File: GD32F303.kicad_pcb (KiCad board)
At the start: 4 copper layers, 127 parts, among them CN1 KF128L-5.08-2P, CN2 WJ15EDGRC-3.81-2P, CN4 WJ15EDGRC-3.81-2P, J1 TYPE-C-31-M-31, J2 TYPE-C 16PIN 2MD(073), Q1 CJ3134K KF, Q2 CJ3134K KF, SW1 SKRPACE010, U1 XL1509-5.0, U10 SIT3485ESA, U11 TXS0104EPWR, U12 TXS0104EPWR, U13 CH340E, U14 TPD4S012DRYR, U2 B0503S-2WR3L, U3 SY8089A1AAC, U4 CH213K, U5 SY8089AAC, U6 GD32F303VCT6, U7 ISO1050DWR, U9 π131U30, Y1 TAXM8M4RDBCCT2T, Y2 XKXGI-SUA-32.768K

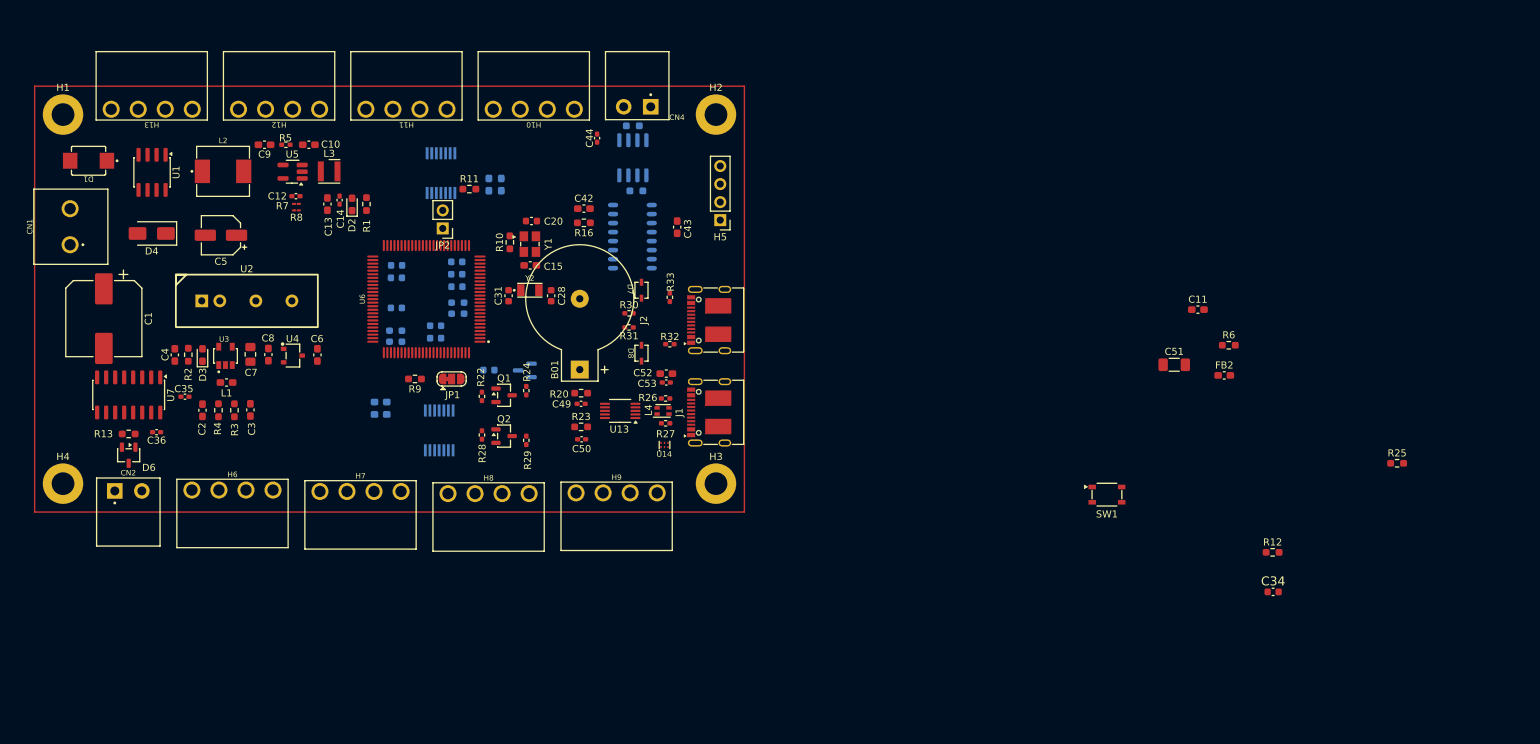
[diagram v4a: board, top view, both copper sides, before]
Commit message: 保存最新器件布局调整
- 归位按键及MCU周边阻容器件
- 调整局部器件方向与丝印位置
- 集中GND与CHASSIS跨接器件等待后续优化
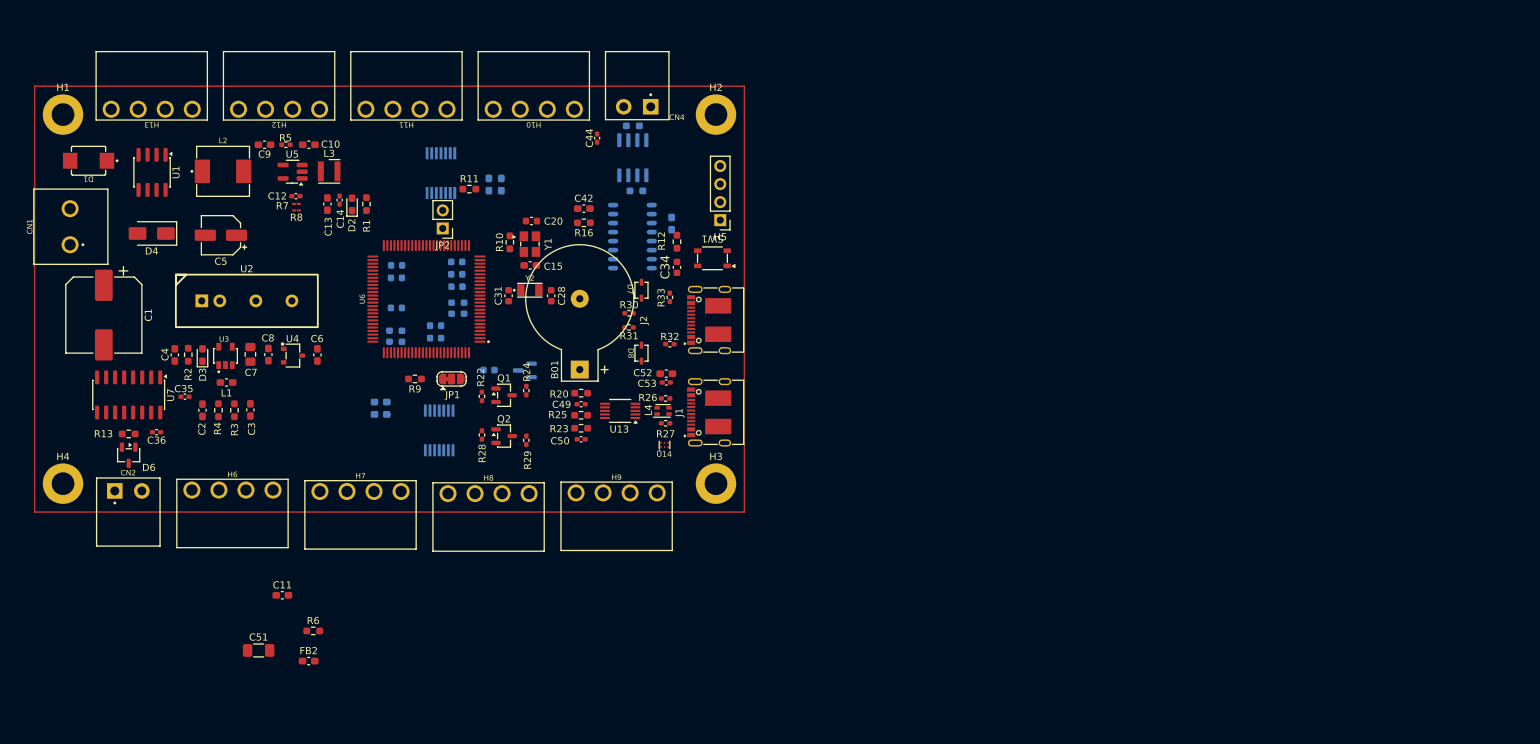
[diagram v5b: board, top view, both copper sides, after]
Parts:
- C43: moved to B.Cu
- moved C51 135.1 mm to (117.1, 138.5)
- moved FB2 135.1 mm to (124.1, 140.0)
- moved R6 135.1 mm to (124.8, 135.8)
- moved C11 135.1 mm to (120.4, 130.7)
- moved R25 115.2 mm to (162.5, 105.4)
- moved C34 95.6 mm to (176.0, 84.5), turned to -90 degrees
- moved R12 94.7 mm to (176.0, 80.9), turned to 90 degrees
- moved SW1 64.8 mm to (181.0, 83.2), turned to 180 degrees
- moved C43 0.93 mm to (175.2, 78.4)
- moved C1 0.50 mm to (95.2, 91.2)
- moved R23 0.19 mm to (162.5, 107.2)
- moved C50 0.07 mm to (162.5, 108.8)
- moved C49 0.06 mm to (162.5, 103.8)

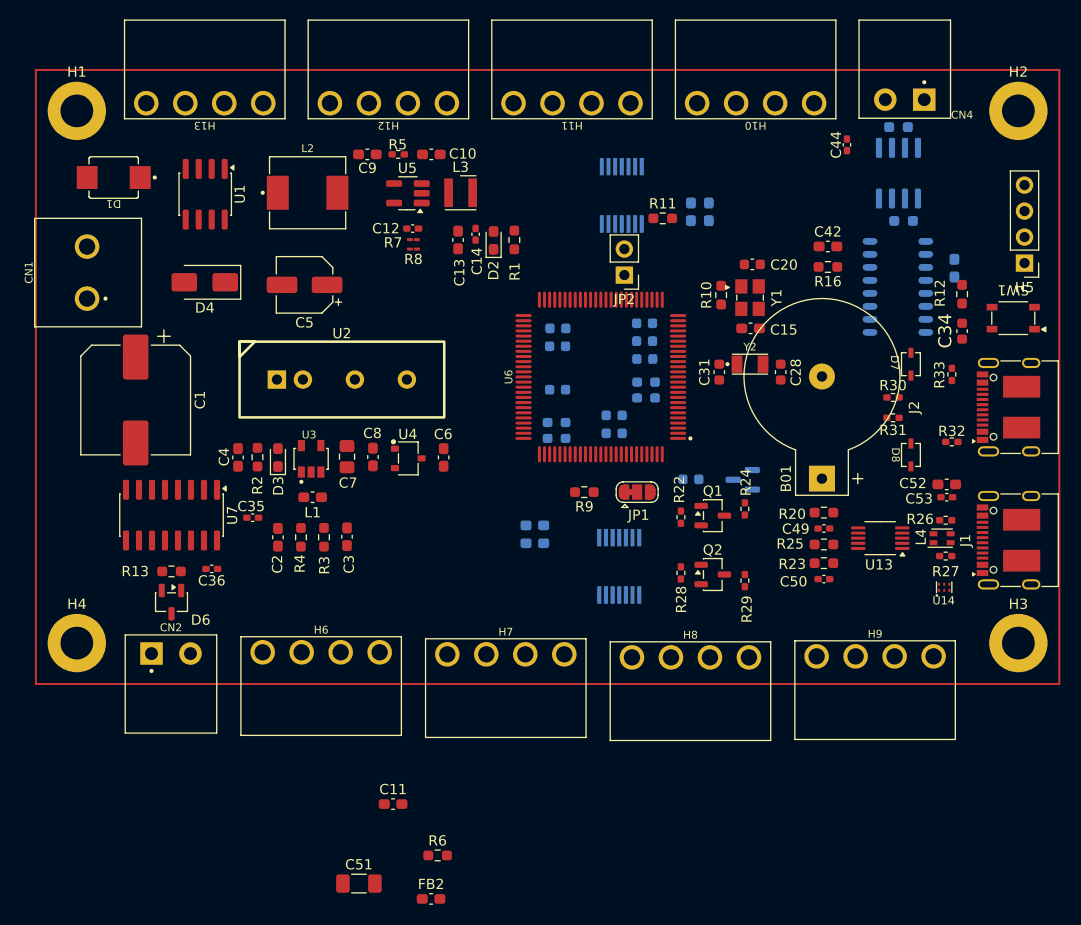
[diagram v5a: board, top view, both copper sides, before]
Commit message: 修复控制总线连接并更新PCB工程文档
规范 PWM、DIR、BRAKE、FG 与 ADC 总线及成员标签，保存最新 PCB 和 KiCad 工程配置，新增工程使用文档。
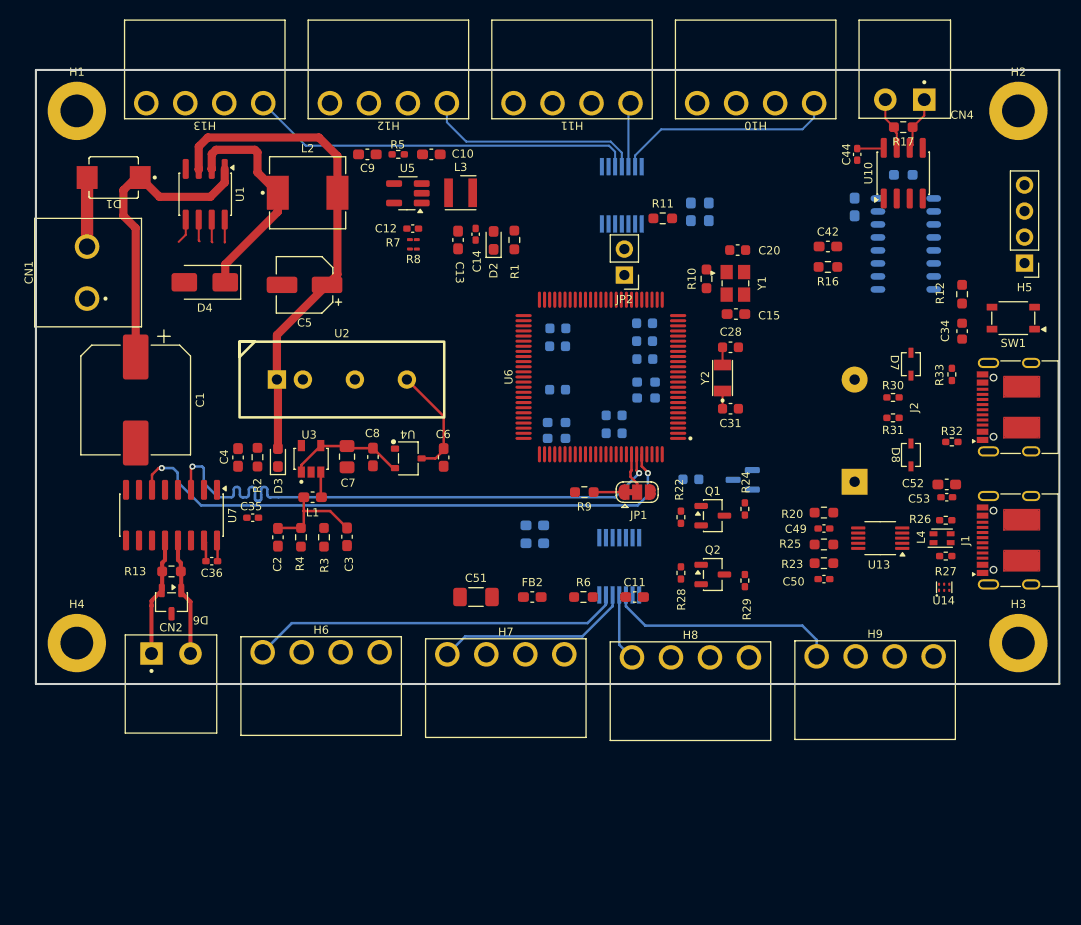
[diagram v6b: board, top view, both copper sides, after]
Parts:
- B01: moved to B.Cu
- R17, U10: moved to F.Cu
- moved FB2 31.1 mm to (134.0, 110.5)
- moved C11 31.1 mm to (144.0, 110.5)
- moved C51 30.2 mm to (128.5, 110.5)
- moved R6 29.0 mm to (139.0, 110.5)
- moved C43 11.4 mm to (165.5, 72.4)
- moved C28 5.47 mm to (153.4, 86.1), turned to 180 degrees
- moved R18 4.50 mm to (170.2, 69.2)
- moved U9 4.27 mm to (170.5, 76.0)
- moved C31 3.74 mm to (153.4, 92.1), turned to 180 degrees
- moved B01 3.21 mm to (165.5, 99.2)
- moved Y2 3.00 mm to (152.6, 89.1), turned to 90 degrees
- moved R10 2.14 mm to (151.0, 79.4)
- moved C15 2.00 mm to (153.9, 82.8)
- moved C20 2.00 mm to (154.1, 76.6)
- moved Y1 2.00 mm to (153.8, 79.8)
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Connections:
- net /MCU_Core/Motor_Comm/PWM1_5V.1 renamed /MCU_Core/Motor_Comm/PWM1_5V_1
- net /MCU_Core/Motor_Comm/PWM1_5V.2 renamed /MCU_Core/Motor_Comm/PWM1_5V_2
- net /MCU_Core/Motor_Comm/PWM1_5V.3 renamed /MCU_Core/Motor_Comm/PWM1_5V_3
- net /MCU_Core/Motor_Comm/PWM1_5V.4 renamed /MCU_Core/Motor_Comm/PWM1_5V_4
- net /MCU_Core/Motor_Comm/PWM2_5V.1 renamed /MCU_Core/Motor_Comm/PWM2_5V_1
- net /MCU_Core/Motor_Comm/PWM2_5V.2 renamed /MCU_Core/Motor_Comm/PWM2_5V_2
- net /MCU_Core/Motor_Comm/PWM2_5V.3 renamed /MCU_Core/Motor_Comm/PWM2_5V_3
- net /MCU_Core/Motor_Comm/PWM2_5V.4 renamed /MCU_Core/Motor_Comm/PWM2_5V_4
- net /MCU_Core/PC0 renamed /MCU_Core/ADC_0
- net /MCU_Core/PC1 renamed /MCU_Core/ADC_1
- net /MCU_Core/PC2 renamed /MCU_Core/ADC_2
- net /MCU_Core/PC3 renamed /MCU_Core/ADC_3
- H10 pad 2: /MCU_Core/Motor_Comm/BRAKE2.1 -> /MCU_Core/BRAKE2_1
- H10 pad 3: /MCU_Core/Motor_Comm/DIR2.1 -> /MCU_Core/DIR2_1
- H10 pad 4: /MCU_Core/Motor_Comm/FG2.1 -> /MCU_Core/FG2_1
- H11 pad 2: /MCU_Core/Motor_Comm/BRAKE2.2 -> /MCU_Core/BRAKE2_2
- H11 pad 3: /MCU_Core/Motor_Comm/DIR2.2 -> /MCU_Core/DIR2_2
- H11 pad 4: /MCU_Core/Motor_Comm/FG2.2 -> /MCU_Core/FG2_2
- H12 pad 2: /MCU_Core/Motor_Comm/BRAKE2.3 -> /MCU_Core/BRAKE2_3
- H12 pad 3: /MCU_Core/Motor_Comm/DIR2.3 -> /MCU_Core/DIR2_3
- H12 pad 4: /MCU_Core/Motor_Comm/FG2.3 -> /MCU_Core/FG2_3
- H13 pad 2: /MCU_Core/Motor_Comm/BRAKE2.4 -> /MCU_Core/BRAKE2_4
- H13 pad 3: /MCU_Core/Motor_Comm/DIR2.4 -> /MCU_Core/DIR2_4
- H13 pad 4: /MCU_Core/Motor_Comm/FG2.4 -> /MCU_Core/FG2_4
- H6 pad 2: /MCU_Core/Motor_Comm/BRAKE1.1 -> /MCU_Core/BRAKE1_1
- H6 pad 3: /MCU_Core/Motor_Comm/DIR1.1 -> /MCU_Core/DIR1_1
- H6 pad 4: /MCU_Core/Motor_Comm/FG1.1 -> /MCU_Core/FG1_1
- H7 pad 2: /MCU_Core/Motor_Comm/BRAKE1.2 -> /MCU_Core/BRAKE1_2
- H7 pad 3: /MCU_Core/Motor_Comm/DIR1.2 -> /MCU_Core/DIR1_2
- H7 pad 4: /MCU_Core/Motor_Comm/FG1.2 -> /MCU_Core/FG1_2
- H8 pad 2: /MCU_Core/Motor_Comm/BRAKE1.3 -> /MCU_Core/BRAKE1_3
- H8 pad 3: /MCU_Core/Motor_Comm/DIR1.3 -> /MCU_Core/DIR1_3
- H8 pad 4: /MCU_Core/Motor_Comm/FG1.3 -> /MCU_Core/FG1_3
- H9 pad 2: /MCU_Core/Motor_Comm/BRAKE1.4 -> /MCU_Core/BRAKE1_4
- H9 pad 3: /MCU_Core/Motor_Comm/DIR1.4 -> /MCU_Core/DIR1_4
- H9 pad 4: /MCU_Core/Motor_Comm/FG1.4 -> /MCU_Core/FG1_4
- U11 pad 2: /MCU_Core/Motor_Comm/PWM1.1 -> /MCU_Core/PWM1_1
- U11 pad 3: /MCU_Core/Motor_Comm/PWM1.2 -> /MCU_Core/PWM1_2
- U11 pad 4: /MCU_Core/Motor_Comm/PWM1.3 -> /MCU_Core/PWM1_3
- U11 pad 5: /MCU_Core/Motor_Comm/PWM1.4 -> /MCU_Core/PWM1_4
- U12 pad 2: /MCU_Core/Motor_Comm/PWM2.1 -> /MCU_Core/PWM2_1
- U12 pad 3: /MCU_Core/Motor_Comm/PWM2.2 -> /MCU_Core/PWM2_2
- U12 pad 4: /MCU_Core/Motor_Comm/PWM2.3 -> /MCU_Core/PWM2_3
- U12 pad 5: /MCU_Core/Motor_Comm/PWM2.4 -> /MCU_Core/PWM2_4
- U6 pad 23: /MCU_Core/PA0 -> /MCU_Core/FG1_1
- U6 pad 24: /MCU_Core/PA1 -> /MCU_Core/FG1_2
- U6 pad 25: /MCU_Core/PA2 -> /MCU_Core/FG1_3
- U6 pad 26: /MCU_Core/PA3 -> /MCU_Core/FG1_4
- U6 pad 31: /MCU_Core/TIMER2_CH0-PWM1 -> /MCU_Core/PWM2_1
- U6 pad 32: /MCU_Core/TIMER2_CH1-PWM2 -> /MCU_Core/PWM2_2
- U6 pad 33: /MCU_Core/PC14 -> /MCU_Core/DIR1_1
- U6 pad 34: /MCU_Core/PC15 -> /MCU_Core/DIR1_2
- U6 pad 35: /MCU_Core/TIMER2_CH2-PWM3 -> /MCU_Core/PWM2_3
- U6 pad 36: /MCU_Core/TIMER2_CH3-PWM4 -> /MCU_Core/PWM2_4
- U6 pad 40: /MCU_Core/TIMER0_CH0-FG1 -> /MCU_Core/FG2_1
- U6 pad 42: /MCU_Core/TIMER0_CH1-FG2 -> /MCU_Core/FG2_2
- U6 pad 44: /MCU_Core/TIMER0_CH2-FG3 -> /MCU_Core/FG2_3
- U6 pad 45: /MCU_Core/TIMER0_CH3-FG4 -> /MCU_Core/FG2_4
- U6 pad 59: /MCU_Core/PD12 -> /MCU_Core/PWM1_1
- U6 pad 60: /MCU_Core/PD13 -> /MCU_Core/PWM1_2
- U6 pad 61: /MCU_Core/PD14 -> /MCU_Core/PWM1_3
- U6 pad 62: /MCU_Core/PD15 -> /MCU_Core/PWM1_4
- U6 pad 63: /MCU_Core/PC6 -> /MCU_Core/DIR1_3
- U6 pad 64: /MCU_Core/PC7 -> /MCU_Core/DIR1_4
- U6 pad 81: /MCU_Core/PD0 -> /MCU_Core/DIR2_1
- U6 pad 82: /MCU_Core/PD1 -> /MCU_Core/DIR2_2
- U6 pad 83: /MCU_Core/PD2 -> /MCU_Core/DIR2_3
- U6 pad 84: /MCU_Core/PD3 -> /MCU_Core/DIR2_4
- U6 pad 85: /MCU_Core/PD4 -> /MCU_Core/BRAKE1_1
- U6 pad 86: /MCU_Core/PD5 -> /MCU_Core/BRAKE1_2
- U6 pad 87: /MCU_Core/PD6 -> /MCU_Core/BRAKE1_3
- U6 pad 88: /MCU_Core/PD7 -> /MCU_Core/BRAKE1_4
- U6 pad 89: /MCU_Core/PB3 -> /MCU_Core/BRAKE2_1
- U6 pad 90: /MCU_Core/PB4 -> /MCU_Core/BRAKE2_2
- U6 pad 91: /MCU_Core/PB5 -> /MCU_Core/BRAKE2_3
- U6 pad 92: /MCU_Core/PB6 -> /MCU_Core/BRAKE2_4
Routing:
- net /MCU_Core/CAN_TX: track 0.00 -> 56.9 mm, vias 0 -> 2
- net /MCU_Core/CAN_RX: track 0.00 -> 56.4 mm, vias 0 -> 2
- net +5V: track 0.00 -> 48.0 mm
- net /MCU_Core/Motor_Comm/PWM2_5V_4: track 0.00 -> 37.8 mm
- net /MCU_Core/Motor_Comm/PWM1_5V_1: track 0.00 -> 36.4 mm
- net Net-(D1-K): track 0.00 -> 29.9 mm
- net /MCU_Core/Motor_Comm/PWM1_5V_4: track 0.00 -> 22.7 mm
- net Net-(D4-K): track 0.00 -> 21.9 mm
- net /MCU_Core/Motor_Comm/PWM2_5V_3: track 0.00 -> 21.5 mm
- net /MCU_Core/Motor_Comm/PWM2_5V_1: track 0.00 -> 21.5 mm
- net /MCU_Core/Motor_Comm/PWM1_5V_2: track 0.00 -> 19.2 mm
- net +5V_ISO: track 0.00 -> 13.6 mm
- net +3V3_ISO: track 0.00 -> 12.9 mm
- net /CAN/CANL: track 0.00 -> 11.6 mm
- net /CAN/CANH: track 0.00 -> 11.6 mm
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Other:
- board outline added: 100 x 60 mm

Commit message: 调整DIR1与DIR2引脚映射并优化局部布局
交换 PD0-PD3 与 PC14、PC15、PC6、PC7 的 DIR1/DIR2 功能分配，同步更新 PCB 网络，并调整 JP2 与 R11 位置。
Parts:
- moved R11 7.84 mm to (138.9, 73.2)
- moved JP2 3.37 mm to (140.5, 76.8), turned to -90 degrees
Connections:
- U6 pad 33: /MCU_Core/DIR1_1 -> /MCU_Core/DIR2_1
- U6 pad 34: /MCU_Core/DIR1_2 -> /MCU_Core/DIR2_2
- U6 pad 63: /MCU_Core/DIR1_3 -> /MCU_Core/DIR2_3
- U6 pad 64: /MCU_Core/DIR1_4 -> /MCU_Core/DIR2_4
- U6 pad 81: /MCU_Core/DIR2_1 -> /MCU_Core/DIR1_1
- U6 pad 82: /MCU_Core/DIR2_2 -> /MCU_Core/DIR1_2
- U6 pad 83: /MCU_Core/DIR2_3 -> /MCU_Core/DIR1_3
- U6 pad 84: /MCU_Core/DIR2_4 -> /MCU_Core/DIR1_4
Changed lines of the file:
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@@
 	(footprint "Connector_PinHeader_2.54mm:PinHeader_1x02_P2.54mm_Vertical"
 		(layer "F.Cu")
-		(at 143 79.04 180)
+		(at 140.525 76.75 -90)
 		(descr "Through hole straight pin header, 1x02, 2.54mm pitch, single row")
 		(tags "Through hole pin header THT 1x02 2.54mm single row")
 		(property "Reference" "JP2"
-			(at 0 -2.38 0)
+			(at 0 -2.38 90)
 			(unlocked yes)
 			(layer "F.SilkS")
@@
 		)
 		(property "Value" "Jumper_2_Small_Open"
-			(at 0 4.92 0)
+			(at 0 4.92 90)
 			(layer "F.Fab")
 			(effects
@@
 		)
 		(property "Datasheet" ""
-			(at 0 0 0)
+			(at 0 0 90)
 			(layer "F.Fab")
 			(hide yes)
@@
 		)
 		(property "Description" "Jumper, 2-pole, small symbol, open"
-			(at 0 0 0)
+			(at 0 0 90)
 			(layer "F.Fab")
 			(hide yes)
@@
 		(duplicate_pad_numbers_are_jumpers no)
 		(fp_line
-			(start 1.38 1.27)
+			(start -1.38 3.92)
 			(end 1.38 3.92)
 			(stroke
@@
 		)
 		(fp_line
-			(start -1.38 3.92)
-			(end 1.38 3.92)
+			(start -1.38 1.27)
+			(end -1.38 3.92)
 			(stroke
 				(width 0.12)
@@
 		)
 		(fp_line
-			(start -1.38 1.27)
-			(end -1.38 3.92)
+			(start 1.38 1.27)
+			(end 1.38 3.92)
 			(stroke
 				(width 0.12)
@@
 		)
 		(fp_line
-			(start 1.27 3.81)
-			(end -1.27 3.81)
+			(start -1.27 3.81)
+			(end -1.27 -0.635)
 			(stroke
 				(width 0.1)
@@
 		)
 		(fp_line
-			(start 1.27 -1.27)
-			(end 1.27 3.81)
+			(start 1.27 3.81)
+			(end -1.27 3.81)
 			(stroke
 				(width 0.1)
@@
 		)
 		(fp_line
-			(start -0.635 -1.27)
-			(end 1.27 -1.27)
+			(start -1.27 -0.635)
+			(end -0.635 -1.27)
 			(stroke
 				(width 0.1)
@@
 		)
 		(fp_line
-			(start -1.27 3.81)
-			(end -1.27 -0.635)
+			(start -0.635 -1.27)
+			(end 1.27 -1.27)
 			(stroke
 				(width 0.1)
@@
 		)
 		(fp_line
-			(start -1.27 -0.635)
-			(end -0.635 -1.27)
+			(start 1.27 -1.27)
+			(end 1.27 3.81)
 			(stroke
 				(width 0.1)
@@
 		)
 		(fp_text user "${REFERENCE}"
-			(at 0 1.27 90)
+			(at 0 1.27 0)
 			(layer "F.Fab")
 			(effects
@@
 		)
 		(pad "1" thru_hole rect
-			(at 0 0 180)
+			(at 0 0 270)
 			(size 1.7 1.7)
 			(drill 1)
@@
 		)
 		(pad "2" thru_hole circle
-			(at 0 2.54 180)
+			(at 0 2.54 270)
 			(size 1.7 1.7)
 			(drill 1)
@@
 	(footprint "Resistor_SMD:R_0603_1608Metric_Pad0.98x0.95mm_HandSolder"
 		(layer "F.Cu")
-		(at 146.75 73.5)
+		(at 138.9125 73.25)
 		(descr "Resistor SMD 0603 (1608 Metric), square (rectangular) end terminal, IPC-7351 nominal with elongated pad for handsoldering. (Body size source: IPC-SM-782 page 72, https://www.pcb-3d.com/wordpress/wp-content/uploads/ipc-sm-782a_amendment_1_and_2.pdf)")
 		(tags "resistor handsolder")
@@
 			(size 1.6 0.3)
 			(layers "F.Cu" "F.Mask" "F.Paste")
-			(net "/MCU_Core/DIR1_1")
+			(net "/MCU_Core/DIR2_1")
 			(pinfunction "DIR1_33")
 			(pintype "bidirectional")
@@
 			(size 1.6 0.3)
 			(layers "F.Cu" "F.Mask" "F.Paste")
-			(net "/MCU_Core/DIR1_2")
+			(net "/MCU_Core/DIR2_2")
 			(pinfunction "DIR2_34")
 			(pintype "bidirectional")
@@
 			(size 0.3 1.6)
 			(layers "F.Cu" "F.Mask" "F.Paste")
-			(net "/MCU_Core/DIR1_3")
+			(net "/MCU_Core/DIR2_3")
 			(pinfunction "DIR3_63")
 			(pintype "bidirectional")
@@
 			(size 0.3 1.6)
 			(layers "F.Cu" "F.Mask" "F.Paste")
-			(net "/MCU_Core/DIR1_4")
+			(net "/MCU_Core/DIR2_4")
 			(pinfunction "DIR4_64")
 			(pintype "bidirectional")
@@
 			(size 1.6 0.3)
 			(layers "F.Cu" "F.Mask" "F.Paste")
-			(net "/MCU_Core/DIR2_1")
+			(net "/MCU_Core/DIR1_1")
 			(pinfunction "PD0_81")
 			(pintype "bidirectional")
@@
 			(size 1.6 0.3)
 			(layers "F.Cu" "F.Mask" "F.Paste")
-			(net "/MCU_Core/DIR2_2")
+			(net "/MCU_Core/DIR1_2")
 			(pinfunction "PD1_82")
 			(pintype "bidirectional")
@@
 			(size 1.6 0.3)
 			(layers "F.Cu" "F.Mask" "F.Paste")
-			(net "/MCU_Core/DIR2_3")
+			(net "/MCU_Core/DIR1_3")
 			(pinfunction "PD2_83")
 			(pintype "bidirectional")
@@
 			(size 1.6 0.3)
 			(layers "F.Cu" "F.Mask" "F.Paste")
-			(net "/MCU_Core/DIR2_4")
+			(net "/MCU_Core/DIR1_4")
 			(pinfunction "PD3_84")
 			(pintype "bidirectional")
